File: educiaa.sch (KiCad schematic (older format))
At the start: 6 parts, among them P10 SPI PORT, P12 ADC PORT, P4 P2 PORT, P5 P1 PORT

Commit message: Cambios menores
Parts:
- added C20: 1nF, Capacitors_SMD:C_1206, symbol C
- added R41: 1M, Resistors_SMD:R_0805, symbol R
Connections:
- net GND: now also C20.1, R41.2
- new net Earth: C20.2, R41.1
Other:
- note added: "Power supplied by\nEDU-CIAA-NXP"
- note added: "Shield to digital ground \nsingle connection point."
- moved on the sheet: C10, C11, P10, P12

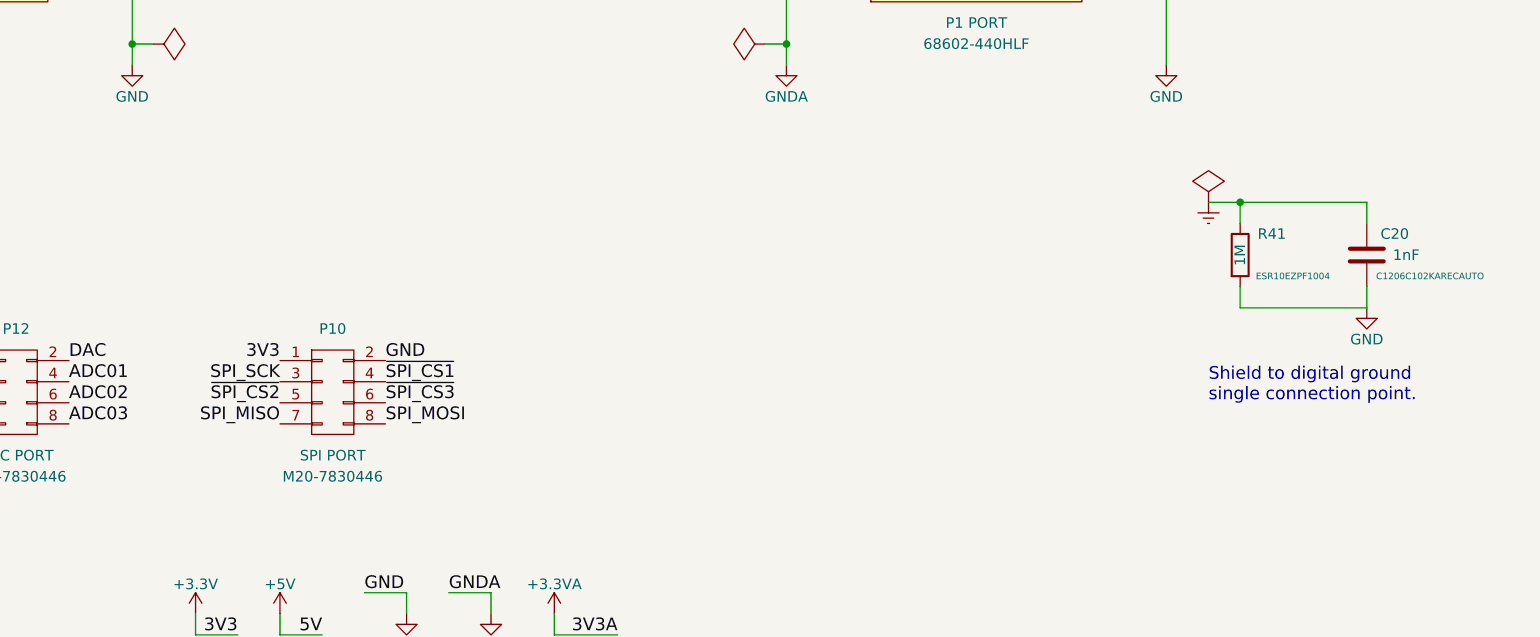
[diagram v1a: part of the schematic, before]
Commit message: Nuevo layout, mejoras y modificaciones del revisor
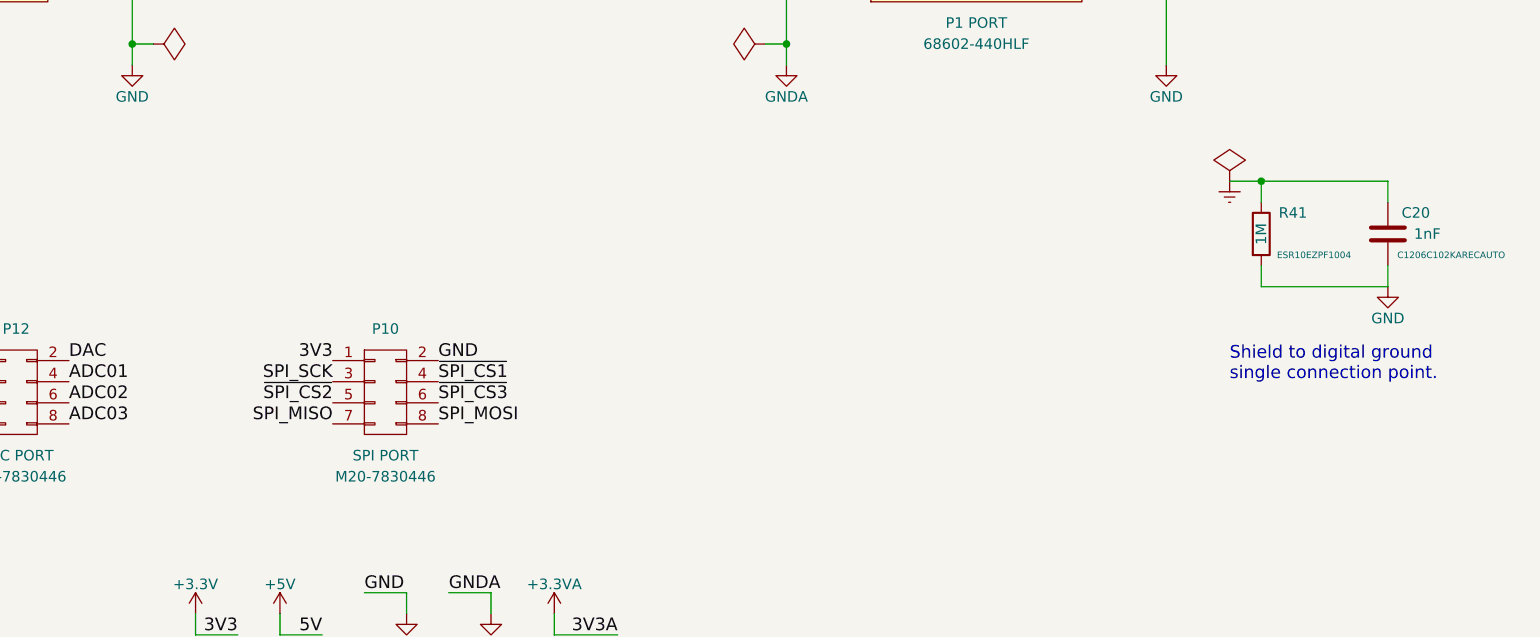
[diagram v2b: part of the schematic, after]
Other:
- moved on the sheet: C20, P10, R41
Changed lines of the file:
@@
 LIBS:contrib
 LIBS:valves
-LIBS:salmon
+LIBS:retro-ciaa
 LIBS:retro-ciaa-cache
 EELAYER 25 0
@@
 encoding utf-8
 Sheet 6 8
-Title "RETRO-CIAA / EDU-CIAA-NXP PORTS"
-Date "2018-10-19"
+Title "EDU-CIAA-NXP INTERFACE"
+Date "2018-10-20"
 Rev "1.1.1"
-Comp "Salmon Robotics"
+Comp "http://www.retro-ciaa.com"
 Comment1 "All resistors 1% & 0603\" unless otherwise noted"
 Comment2 "ERC check OK on 2018-10-19"
@@
 NoConn ~ 9200 3500
 NoConn ~ 9200 2300
-Text Label 5100 6200 2    60   ~ 0
+Text Label 5350 6200 2    60   ~ 0
 3V3
-Text Label 5600 6200 0    60   ~ 0
+Text Label 5850 6200 0    60   ~ 0
 GND
 Text Label 2700 2600 2    60   ~ 0
 SPI_MISO
-Text Label 5100 6500 2    60   ~ 0
+Text Label 5350 6500 2    60   ~ 0
 SPI_MISO
 Text Label 2700 2700 2    60   ~ 0
 SPI_SCK
-Text Label 5100 6300 2    60   ~ 0
+Text Label 5350 6300 2    60   ~ 0
 SPI_SCK
 Text Label 2700 2500 2    60   ~ 0
 SPI_MOSI
-Text Label 5600 6500 0    60   ~ 0
+Text Label 5850 6500 0    60   ~ 0
 SPI_MOSI
 Text Label 4300 2500 0    60   ~ 0
 ~SPI_CS3
-Text Label 5600 6300 0    60   ~ 0
+Text Label 5850 6300 0    60   ~ 0
 ~SPI_CS1
 $Comp
 L CONN_02X04 P10
 U 1 1 5BD3FED6
-P 5350 6350
-F 0 "P10" H 5350 6650 50  0000 C CNN
-F 1 "SPI PORT" H 5350 6050 50  0000 C CNN
-F 2 "Pin_Headers:Pin_Header_Straight_2x04_Pitch2.54mm" H 5350 5150 50  0001 C CNN
-F 3 "M20-7830446" H 5350 5950 50  0000 C CNN
-	1    5350 6350
+P 5600 6350
+F 0 "P10" H 5600 6650 50  0000 C CNN
+F 1 "SPI PORT" H 5600 6050 50  0000 C CNN
+F 2 "Pin_Headers:Pin_Header_Straight_2x04_Pitch2.54mm" H 5600 5150 50  0001 C CNN
+F 3 "M20-7830446" H 5600 5950 50  0000 C CNN
+	1    5600 6350
 	1    0    0    -1
 $EndComp
@@
 Text Label 4300 3100 0    60   ~ 0
 ~SPI_CS1
-Text Label 5100 6400 2    60   ~ 0
+Text Label 5350 6400 2    60   ~ 0
 ~SPI_CS2
-Text Label 5600 6400 0    60   ~ 0
+Text Label 5850 6400 0    60   ~ 0
 ~SPI_CS3
 NoConn ~ 4300 2700
@@
 L C C20
 U 1 1 5BCB1922
-P 10250 5700
-F 0 "C20" H 10050 5600 50  0000 L CNN
-F 1 "1nF" H 10000 5700 50  0000 L CNN
-F 2 "Capacitors_SMD:C_1206" H 10250 5700 31  0001 C CNN
-F 3 "C1206C102KARECAUTO" H 9950 5800 31  0000 C CNN
-	1    10250 5700
+P 10350 5600
+F 0 "C20" H 10150 5500 50  0000 L CNN
+F 1 "1nF" H 10100 5600 50  0000 L CNN
+F 2 "Capacitors_SMD:C_1206" H 10350 5600 31  0001 C CNN
+F 3 "C1206C102KARECAUTO" H 10050 5700 31  0000 C CNN
+	1    10350 5600
 	-1   0    0    1
 $EndComp
@@
 L R R41
 U 1 1 5BCB1929
-P 9650 5700
-F 0 "R41" H 9800 5800 50  0000 C CNN
-F 1 "1M" V 9650 5700 50  0000 C CNN
-F 2 "Resistors_SMD:R_0805" V 9580 5700 31  0001 C CNN
-F 3 "ESR10EZPF1004" H 9900 5600 31  0000 C CNN
-	1    9650 5700
+P 9750 5600
+F 0 "R41" H 9900 5700 50  0000 C CNN
+F 1 "1M" V 9750 5600 50  0000 C CNN
+F 2 "Resistors_SMD:R_0805" V 9680 5600 31  0001 C CNN
+F 3 "ESR10EZPF1004" H 10000 5500 31  0000 C CNN
+	1    9750 5600
 	1    0    0    -1
 $EndComp
@@
 L GND #PWR076
 U 1 1 5BCB1930
-P 10250 5950
-F 0 "#PWR076" H 10250 5700 50  0001 C CNN
-F 1 "GND" H 10250 5800 50  0000 C CNN
-F 2 "" H 10250 5950 50  0000 C CNN
-F 3 "" H 10250 5950 50  0000 C CNN
-	1    10250 5950
+P 10350 5850
+F 0 "#PWR076" H 10350 5600 50  0001 C CNN
+F 1 "GND" H 10350 5700 50  0000 C CNN
+F 2 "" H 10350 5850 50  0000 C CNN
+F 3 "" H 10350 5850 50  0000 C CNN
+	1    10350 5850
 	1    0    0    -1
 $EndComp
@@
 L Earth #PWR077
 U 1 1 5BCB1936
-P 9500 5450
-F 0 "#PWR077" H 9500 5200 50  0001 C CNN
-F 1 "Earth" H 9500 5300 50  0001 C CNN
-F 2 "" H 9500 5450 50  0000 C CNN
-F 3 "" H 9500 5450 50  0000 C CNN
-	1    9500 5450
+P 9600 5350
+F 0 "#PWR077" H 9600 5100 50  0001 C CNN
+F 1 "Earth" H 9600 5200 50  0001 C CNN
+F 2 "" H 9600 5350 50  0000 C CNN
+F 3 "" H 9600 5350 50  0000 C CNN
+	1    9600 5350
 	1    0    0    -1
 $EndComp
@@
 L PWR_FLAG #FLG078
 U 1 1 5BCB193C
-P 9500 5450
-F 0 "#FLG078" H 9500 5545 50  0001 C CNN
-F 1 "PWR_FLAG" H 9500 5630 50  0001 C CNN
-F 2 "" H 9500 5450 50  0000 C CNN
-F 3 "" H 9500 5450 50  0000 C CNN
-	1    9500 5450
-	1    0    0    -1
-$EndComp
-Wire Wire Line
-	9650 5450 9650 5550
-Wire Wire Line
-	9650 5850 9650 5950
-Wire Wire Line
-	9650 5950 10250 5950
-Wire Wire Line
-	10250 5950 10250 5850
-Wire Wire Line
-	9500 5450 10250 5450
-Connection ~ 9650 5450
-Wire Wire Line
-	10250 5450 10250 5550
-Text Notes 9500 6400 0    60   ~ 0
+P 9600 5350
+F 0 "#FLG078" H 9600 5445 50  0001 C CNN
+F 1 "PWR_FLAG" H 9600 5530 50  0001 C CNN
+F 2 "" H 9600 5350 50  0000 C CNN
+F 3 "" H 9600 5350 50  0000 C CNN
+	1    9600 5350
+	1    0    0    -1
+$EndComp
+Wire Wire Line
+	9750 5350 9750 5450
+Wire Wire Line
+	9750 5750 9750 5850
+Wire Wire Line
+	9750 5850 10350 5850
+Wire Wire Line
+	10350 5850 10350 5750
+Wire Wire Line
+	9600 5350 10350 5350
+Connection ~ 9750 5350
+Wire Wire Line
+	10350 5350 10350 5450
+Text Notes 9600 6300 0    60   ~ 0
 Shield to digital ground \nsingle connection point.
 $EndSCHEMATC

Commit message: Limpieza de etiquetas de alimentacion
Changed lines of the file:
@@
 NoConn ~ 9200 2500
 $Comp
-L +3.3V #PWR056
+L +3.3V #PWR051
 U 1 1 5BD3FE6A
 P 2600 1800
-F 0 "#PWR056" H 2600 1650 50  0001 C CNN
+F 0 "#PWR051" H 2600 1650 50  0001 C CNN
 F 1 "+3.3V" H 2600 1940 50  0000 C CNN
 F 2 "" H 2600 1800 50  0000 C CNN
@@
 $EndComp
 $Comp
-L +5V #PWR057
+L +5V #PWR052
 U 1 1 5BD3FE70
 P 2300 1800
-F 0 "#PWR057" H 2300 1650 50  0001 C CNN
+F 0 "#PWR052" H 2300 1650 50  0001 C CNN
 F 1 "+5V" H 2300 1940 50  0000 C CNN
 F 2 "" H 2300 1800 50  0000 C CNN
@@
 $EndComp
 $Comp
-L PWR_FLAG #FLG058
+L PWR_FLAG #FLG053
 U 1 1 5BD3FE76
 P 2700 1900
-F 0 "#FLG058" H 2700 1995 50  0001 C CNN
+F 0 "#FLG053" H 2700 1995 50  0001 C CNN
 F 1 "PWR_FLAG" H 2700 2080 50  0001 C CNN
 F 2 "" H 2700 1900 50  0000 C CNN
@@
 $EndComp
 $Comp
-L PWR_FLAG #FLG059
+L PWR_FLAG #FLG054
 U 1 1 5BD3FE7C
 P 2200 1900
-F 0 "#FLG059" H 2200 1995 50  0001 C CNN
+F 0 "#FLG054" H 2200 1995 50  0001 C CNN
 F 1 "PWR_FLAG" H 2200 2080 50  0001 C CNN
 F 2 "" H 2200 1900 50  0000 C CNN
@@
 $EndComp
 $Comp
-L PWR_FLAG #FLG060
+L PWR_FLAG #FLG055
 U 1 1 5BD3FE82
 P 7400 4700
-F 0 "#FLG060" H 7400 4795 50  0001 C CNN
+F 0 "#FLG055" H 7400 4795 50  0001 C CNN
 F 1 "PWR_FLAG" H 7400 4880 50  0001 C CNN
 F 2 "" H 7400 4700 50  0000 C CNN
@@
 $EndComp
 $Comp
-L PWR_FLAG #FLG061
+L PWR_FLAG #FLG056
 U 1 1 5BD3FE88
 P 7600 1900
-F 0 "#FLG061" H 7600 1995 50  0001 C CNN
+F 0 "#FLG056" H 7600 1995 50  0001 C CNN
 F 1 "PWR_FLAG" H 7600 2080 50  0001 C CNN
 F 2 "" H 7600 1900 50  0000 C CNN
@@
 $EndComp
 $Comp
-L GND #PWR062
+L GND #PWR057
 U 1 1 5BD3FE8E
 P 9300 4800
-F 0 "#PWR062" H 9300 4550 50  0001 C CNN
+F 0 "#PWR057" H 9300 4550 50  0001 C CNN
 F 1 "GND" H 9300 4650 50  0000 C CNN
 F 2 "" H 9300 4800 50  0000 C CNN
@@
 $EndComp
 $Comp
-L PWR_FLAG #FLG063
+L PWR_FLAG #FLG058
 U 1 1 5BD3FE94
 P 4500 4700
-F 0 "#FLG063" H 4500 4795 50  0001 C CNN
+F 0 "#FLG058" H 4500 4795 50  0001 C CNN
 F 1 "PWR_FLAG" H 4500 4880 50  0001 C CNN
 F 2 "" H 4500 4700 50  0000 C CNN
@@
 $EndComp
 $Comp
-L GND #PWR064
+L GND #PWR059
 U 1 1 5BD3FEA6
 P 1700 6900
-F 0 "#PWR064" H 1700 6650 50  0001 C CNN
+F 0 "#PWR059" H 1700 6650 50  0001 C CNN
 F 1 "GND" H 1700 6750 50  0000 C CNN
 F 2 "" H 1700 6900 50  0000 C CNN
@@
 $EndComp
 $Comp
-L +3.3V #PWR065
+L +3.3V #PWR060
 U 1 1 5BD3FEAC
 P 1700 6400
-F 0 "#PWR065" H 1700 6250 50  0001 C CNN
+F 0 "#PWR060" H 1700 6250 50  0001 C CNN
 F 1 "+3.3V" H 1700 6540 50  0000 C CNN
 F 2 "" H 1700 6400 50  0000 C CNN
@@
 $EndComp
 $Comp
-L GND #PWR066
+L GND #PWR061
 U 1 1 5BD3FEB9
 P 2400 6900
-F 0 "#PWR066" H 2400 6650 50  0001 C CNN
+F 0 "#PWR061" H 2400 6650 50  0001 C CNN
 F 1 "GND" H 2400 6750 50  0000 C CNN
 F 2 "" H 2400 6900 50  0000 C CNN
@@
 $EndComp
 $Comp
-L +5V #PWR067
+L +5V #PWR062
 U 1 1 5BD3FEBF
 P 2400 6400
-F 0 "#PWR067" H 2400 6250 50  0001 C CNN
+F 0 "#PWR062" H 2400 6250 50  0001 C CNN
 F 1 "+5V" H 2400 6540 50  0000 C CNN
 F 2 "" H 2400 6400 50  0000 C CNN
@@
 P1 & P2 ports are the I/O interface\nto -and power supply from- the \nEDU-CIAA-NXP board
 $Comp
-L +3.3VA #PWR068
+L +3.3VA #PWR063
 U 1 1 5BD3FEF7
 P 7500 1800
-F 0 "#PWR068" H 7500 1650 50  0001 C CNN
+F 0 "#PWR063" H 7500 1650 50  0001 C CNN
 F 1 "+3.3VA" H 7500 1940 50  0000 C CNN
 F 2 "" H 7500 1800 50  0000 C CNN
@@
 $EndComp
 $Comp
-L GNDA #PWR069
+L GNDA #PWR064
 U 1 1 5BD3FEFD
 P 7500 4800
-F 0 "#PWR069" H 7500 4550 50  0001 C CNN
+F 0 "#PWR064" H 7500 4550 50  0001 C CNN
 F 1 "GNDA" H 7500 4650 50  0000 C CNN
 F 2 "" H 7500 4800 50  0000 C CNN
@@
 $EndComp
 $Comp
-L GND #PWR070
+L GND #PWR065
 U 1 1 5BD3FF03
 P 4400 4800
-F 0 "#PWR070" H 4400 4550 50  0001 C CNN
+F 0 "#PWR065" H 4400 4550 50  0001 C CNN
 F 1 "GND" H 4400 4650 50  0000 C CNN
 F 2 "" H 4400 4800 50  0000 C CNN
@@
 R2
 $Comp
-L +3.3VA #PWR071
+L +3.3VA #PWR066
 U 1 1 5BDCEB84
 P 6400 7400
-F 0 "#PWR071" H 6400 7250 50  0001 C CNN
+F 0 "#PWR066" H 6400 7250 50  0001 C CNN
 F 1 "+3.3VA" H 6400 7540 50  0000 C CNN
 F 2 "" H 6400 7400 50  0000 C CNN
@@
 $EndComp
 $Comp
-L GNDA #PWR072
+L GNDA #PWR067
 U 1 1 5BDCEB8A
 P 6100 7400
-F 0 "#PWR072" H 6100 7150 50  0001 C CNN
+F 0 "#PWR067" H 6100 7150 50  0001 C CNN
 F 1 "GNDA" H 6100 7250 50  0000 C CNN
 F 2 "" H 6100 7400 50  0000 C CNN
@@
 GNDA
 Text Label 5300 7500 2    60   ~ 0
-5V
-Text Label 4900 7500 2    60   ~ 0
 3V3
 Text Label 6700 7500 2    60   ~ 0
 3V3A
 $Comp
-L +5V #PWR073
-U 1 1 5BDCEB94
+L +3.3V #PWR068
+U 1 1 5BDCEB9A
 P 5100 7400
-F 0 "#PWR073" H 5100 7250 50  0001 C CNN
-F 1 "+5V" H 5100 7540 50  0000 C CNN
+F 0 "#PWR068" H 5100 7250 50  0001 C CNN
+F 1 "+3.3V" H 5100 7540 50  0000 C CNN
 F 2 "" H 5100 7400 50  0000 C CNN
 F 3 "" H 5100 7400 50  0000 C CNN
@@
 $EndComp
 $Comp
-L +3.3V #PWR074
-U 1 1 5BDCEB9A
-P 4700 7400
-F 0 "#PWR074" H 4700 7250 50  0001 C CNN
-F 1 "+3.3V" H 4700 7540 50  0000 C CNN
-F 2 "" H 4700 7400 50  0000 C CNN
-F 3 "" H 4700 7400 50  0000 C CNN
-	1    4700 7400
-	1    0    0    -1
-$EndComp
-$Comp
-L GND #PWR075
+L GND #PWR069
 U 1 1 5BDCEBA0
 P 5700 7400
-F 0 "#PWR075" H 5700 7150 50  0001 C CNN
+F 0 "#PWR069" H 5700 7150 50  0001 C CNN
 F 1 "GND" H 5700 7250 50  0000 C CNN
 F 2 "" H 5700 7400 50  0000 C CNN
@@
 Text Label 5500 7300 0    60   ~ 0
 GND
-Wire Wire Line
-	4700 7400 4700 7500
-Wire Wire Line
-	4700 7500 4900 7500
 Wire Wire Line
 	5100 7400 5100 7500
@@
 $EndComp
 $Comp
-L GND #PWR076
+L GND #PWR070
 U 1 1 5BCB1930
 P 10350 5850
-F 0 "#PWR076" H 10350 5600 50  0001 C CNN
+F 0 "#PWR070" H 10350 5600 50  0001 C CNN
 F 1 "GND" H 10350 5700 50  0000 C CNN
 F 2 "" H 10350 5850 50  0000 C CNN
@@
 $EndComp
 $Comp
-L Earth #PWR077
+L Earth #PWR071
 U 1 1 5BCB1936
 P 9600 5350
-F 0 "#PWR077" H 9600 5100 50  0001 C CNN
+F 0 "#PWR071" H 9600 5100 50  0001 C CNN
 F 1 "Earth" H 9600 5200 50  0001 C CNN
 F 2 "" H 9600 5350 50  0000 C CNN
@@
 $EndComp
 $Comp
-L PWR_FLAG #FLG078
+L PWR_FLAG #FLG072
 U 1 1 5BCB193C
 P 9600 5350
-F 0 "#FLG078" H 9600 5445 50  0001 C CNN
+F 0 "#FLG072" H 9600 5445 50  0001 C CNN
 F 1 "PWR_FLAG" H 9600 5530 50  0001 C CNN
 F 2 "" H 9600 5350 50  0000 C CNN
